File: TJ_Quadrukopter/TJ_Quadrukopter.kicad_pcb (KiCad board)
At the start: 2 copper layers, 16 parts, among them M1 Motor_DC, M2 Motor_DC, M3 Motor_DC, M4 Motor_DC, Q1 IRF540N, Q2 IRF540N, Q3 IRF540N, Q4 IRF540N, U1 HC-06, U2 MPU6050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

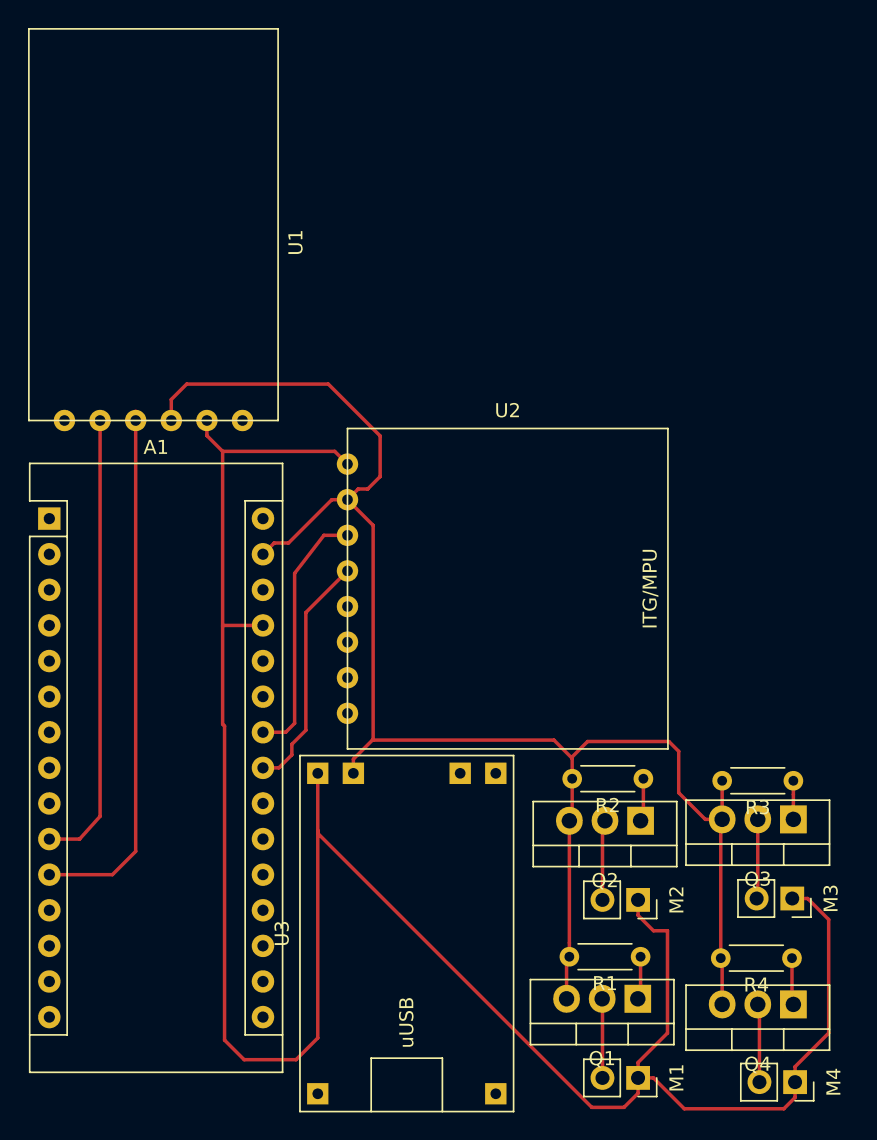
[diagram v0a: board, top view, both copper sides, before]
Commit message: Added original specification from Timko and also mproved board, now it's more compact and its about 5x7cm big.
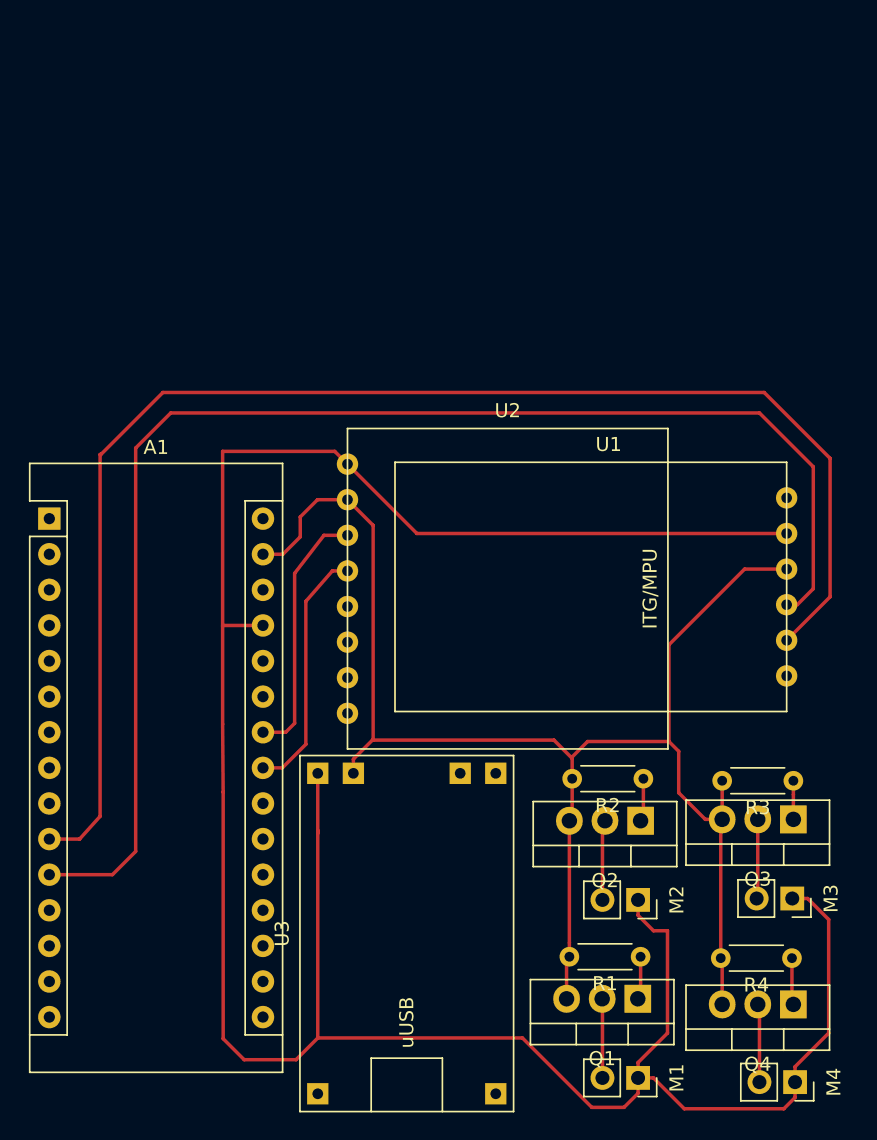
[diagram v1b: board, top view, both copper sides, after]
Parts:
- moved U1 38.9 mm to (154.5, 41.7), turned to 180 degrees
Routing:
- net Net-(A1-Pad10): track 32.6 -> 100.3 mm
- net Net-(A1-Pad11): track 38.2 -> 97.7 mm
- net Net-(A1-Pad27): track 160.7 -> 185.4 mm
- net Net-(A1-Pad29): track 116.2 -> 110.3 mm
- net Net-(A1-Pad23): track 17.2 -> 17.9 mm

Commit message: Added 3D models for arduino and connect them inside KiCADe, I have placed them before on differen drive path so maybe this will not shown correctly, but all used models and everything is here.
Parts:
- A1: footprint Module:Arduino_Nano -> LuboJ_footprints:Arduino_Nano
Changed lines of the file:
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@@
   (module LuboJ_footprints:HC-06 (layer F.Cu)
     (at 154.5 41.7 180)
-    (fp_text reference U1 (at 0 8.89) (layer F.SilkS)
+    (fp_text reference U1 (at 0 8.89 180) (layer F.SilkS)
       (effects (font (size 1 1) (thickness 0.15)))
     )
-    (fp_text value HC-06 (at 0 -11.43) (layer F.Fab)
+    (fp_text value HC-06 (at 0 -11.43 180) (layer F.Fab)
       (effects (font (size 1 1) (thickness 0.15)))
     )
-    (fp_line (start -12.7 7.62) (end -12.7 -10.16) (layer F.SilkS) (width 0.12))
-    (fp_line (start 15.24 7.62) (end -12.7 7.62) (layer F.SilkS) (width 0.12))
+    (fp_line (start -13.97 7.62) (end -13.97 -10.16) (layer F.SilkS) (width 0.12))
+    (fp_line (start 15.24 7.62) (end -13.97 7.62) (layer F.SilkS) (width 0.12))
     (fp_line (start 15.24 -10.16) (end 15.24 7.62) (layer F.SilkS) (width 0.12))
-    (fp_line (start -12.7 -10.16) (end 15.24 -10.16) (layer F.SilkS) (width 0.12))
+    (fp_line (start -13.97 -10.16) (end 15.24 -10.16) (layer F.SilkS) (width 0.12))
     (pad 6 thru_hole circle (at -12.7 5.08 180) (size 1.524 1.524) (drill 0.762) (layers *.Cu *.Mask)
       (net 31 "Net-(U1-Pad6)"))
@@
     (pad 1 thru_hole circle (at -12.7 -7.62 180) (size 1.524 1.524) (drill 0.762) (layers *.Cu *.Mask)
       (net 32 "Net-(U1-Pad1)"))
+    (model C:/Users/H364387/Documents/KiCad/LuboJ_libs/hc-06/BluetoothModul_HC06.wrl
+      (offset (xyz 0 1.5 2))
+      (scale (xyz 0.3 0.3 0.4))
+      (rotate (xyz 0 0 0))
+    )
+    (model C:/Users/H364387/Documents/KiCad/LuboJ_libs/3d_models/hc-06/BluetoothModul_HC06.wrl
+      (offset (xyz 0 1.5 2))
+      (scale (xyz 0.3 0.3 0.4))
+      (rotate (xyz -90 0 0))
+    )
   )
-  (module Module:Arduino_Nano (layer F.Cu)
+  (module LuboJ_footprints:Arduino_Nano (layer F.Cu)
     (at 114.6 38.1)
     (descr "Arduino Nano, http://www.mouser.com/pdfdocs/Gravitech_Arduino_Nano3_0.pdf")
@@
       (rotate (xyz 0 0 0))
     )
+    (model C:/Users/H364387/Documents/KiCad/LuboJ_libs/3d_models/arduino_nano/arduino_nano.wrl
+      (offset (xyz 7.5 -17.7 2.5))
+      (scale (xyz 0.385 0.385 0.385))
+      (rotate (xyz -90 0 90))
+    )
   )
